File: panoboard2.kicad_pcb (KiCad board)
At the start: 2 copper layers, 100 x 69.6 mm, 69 parts, among them J11 I2C1, J12 I2C2, J2 THERMISTOR, J6 BLK/MAINS L, J7 WHT/HTR, J8 ORA/MAINS N, J9 MOLEX 53375-0810, K1 Relay_SPDT, M2 TINYPICO, P2 PCB_Patch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

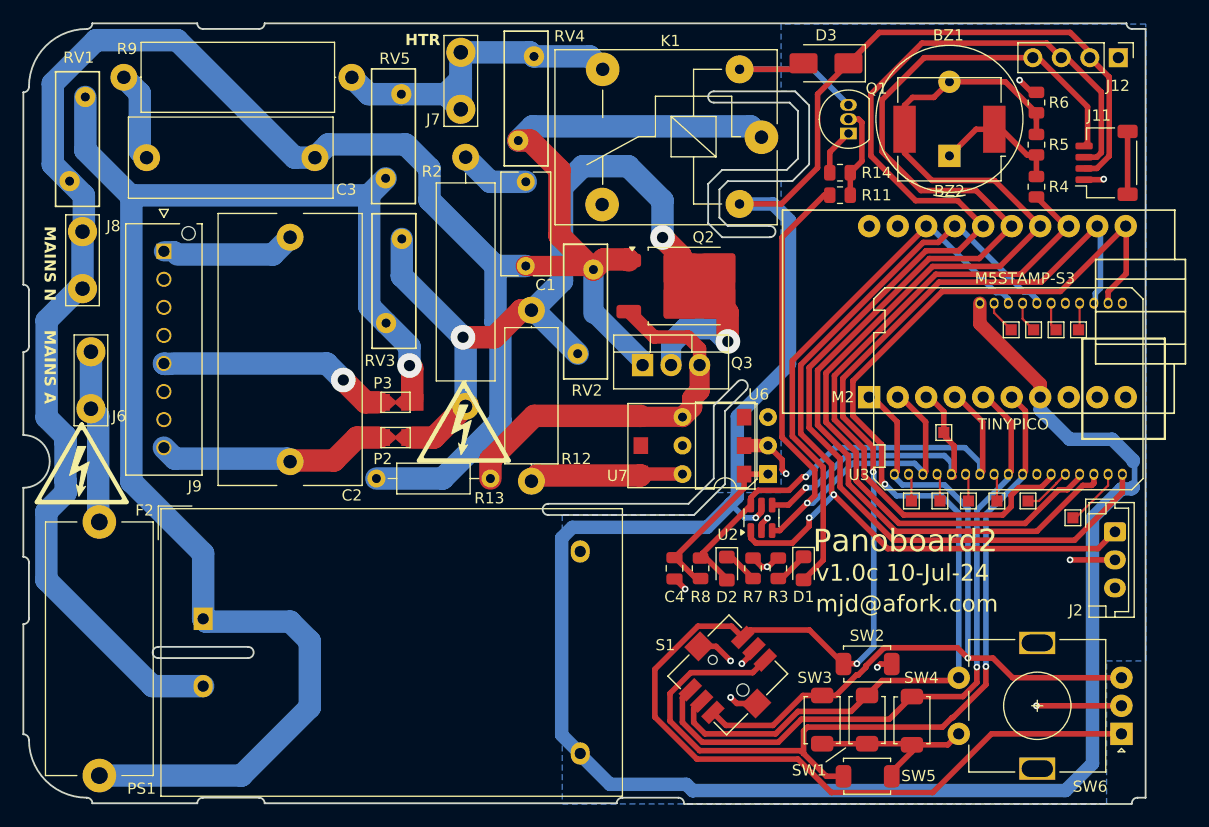
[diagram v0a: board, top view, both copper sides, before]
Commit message: Many improvements
Moved fuse to the neutral line so heater is protected
Added slot under R2
Moved mounting hole
Improved board outline
Added OSHW licence and KiCad shout-out
Fixed buzzer pin pitch
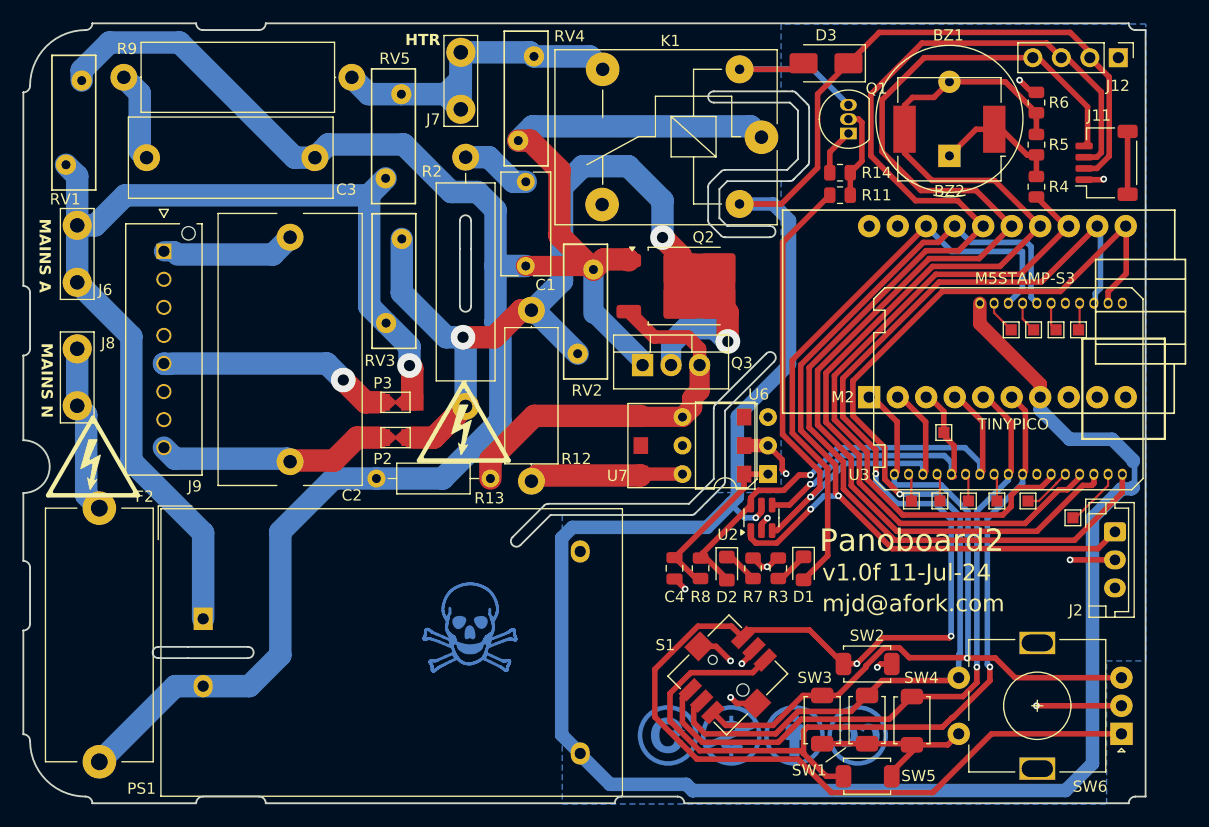
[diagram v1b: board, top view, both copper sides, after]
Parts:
- added REF**: Symbol_CC-Noncommercial_CopperTop_Small, Symbol:Symbol_CC-Noncommercial_CopperTop_Small, B.Cu at (113.1, 93.5)
- added REF**: Symbol_CC-Attribution_CopperTop_Small, Symbol:Symbol_CC-Attribution_CopperTop_Small, B.Cu at (118.7, 93.5)
- added REF**: Symbol_CC-ShareAlike_CopperTop_Small, Symbol:Symbol_CC-ShareAlike_CopperTop_Small, B.Cu at (107.5, 93.5)
- added REF**: OSHW-Logo_5.7x6mm_SilkScreen, Symbol:OSHW-Logo_5.7x6mm_SilkScreen, B.Cu at (107.9, 83.3)
- added REF**: Symbol_Danger_8x8mm_Copper, Symbol:Symbol_Danger_8x8mm_Copper, B.Cu at (89.8, 83.8)
- added REF**: KiCad-Logo2_6mm_SilkScreen, local:KiCad-Logo2_6mm_SilkScreen, B.Cu at (119.7, 83.9)
- added REF**: Symbol_CreativeCommons_CopperTop_Type2_Small, Symbol:Symbol_CreativeCommons_CopperTop_Type2_Small, B.Cu at (124.3, 93.5)
- moved REF** 25.6 mm to (66.0, 74.3)
- moved J6 11.3 mm to (54.8, 48.0)
- moved J8 10.5 mm to (54.8, 59.0)
- moved RV1 6.28 mm to (53.8, 42.6), turned to 90 degrees
- moved F2 1.23 mm to (56.8, 73.2)
- moved REF** 1.17 mm to (56.2, 68.6)
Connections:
- F2 pad 1: Net-(J6-Pin_1) -> Net-(J8-Pin_1)
- F2 pad 2: MAINS_A -> MAINS_N
- J6 pad 1: Net-(J6-Pin_1) -> MAINS_A
- J8 pad 1: MAINS_N -> Net-(J8-Pin_1)
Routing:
- net MAINS_A: track 131.5 -> 94.6 mm
- net MAINS_N: track 206.0 -> 180.2 mm
- net Net-(J6-Pin_1): track 15.5 -> 0.00 mm
- net Net-(J8-Pin_1): track 0.00 -> 15.0 mm
- net /SW2: track 135.0 -> 146.2 mm, vias 2 -> 3
- net /LED: track 48.7 -> 53.3 mm
- net /THERM: track 80.1 -> 82.3 mm
- net /MTR_N: track 77.8 -> 78.6 mm
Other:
- board size 100 x 69.6 mm -> 100 x 69.5 mm
- board text added: ":-)"
- board text added: "CC BY-NC-SA 4.0"
- board text added: "v1.0f 11-Jul-24"
- board text removed: "v1.0c 10-Jul-24"

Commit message: Removed a rebate because there's a support under it.
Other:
- outline, holes or cut-outs redrawn
- board text added: "v1.0g 11-Jul-24"
- board text removed: "v1.0f 11-Jul-24"

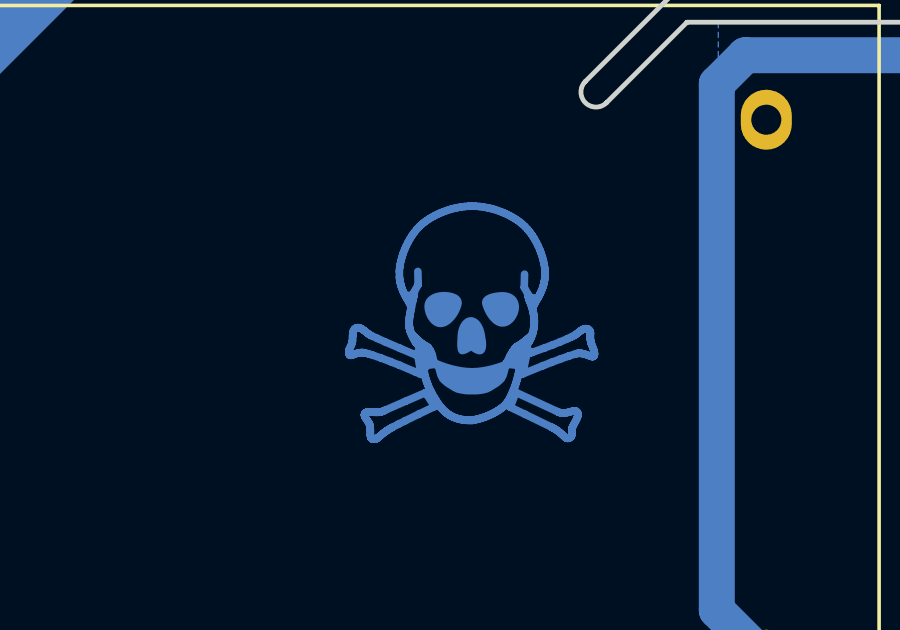
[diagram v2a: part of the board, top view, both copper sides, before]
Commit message: Moved soldermask no-mans-land to match new slots.
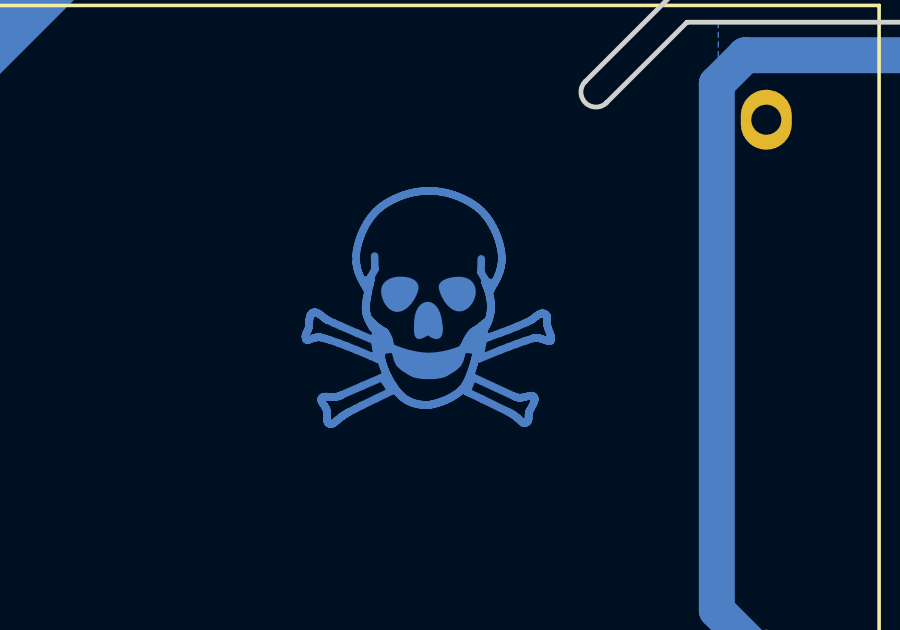
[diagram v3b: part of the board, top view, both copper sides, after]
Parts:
- moved REF** 1.53 mm to (88.4, 83.2)
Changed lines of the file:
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@@
 			(usegerberattributes yes)
 			(usegerberadvancedattributes yes)
-			(creategerberjobfile yes)
+			(creategerberjobfile no)
 			(dashed_line_dash_ratio 12.000000)
 			(dashed_line_gap_ratio 3.000000)
@@
 	(footprint "Symbol:Symbol_Danger_8x8mm_Copper"
 		(layer "B.Cu")
-		(at 89.813608 83.75865 180)
+		(at 88.371392 83.248157 180)
 		(descr "Danger symbol, 8x8mm, copper layer")
 		(tags "warning graphic")
@@
 	)
 	(gr_line
-		(start 114.022216 62.310493)
-		(end 116.522216 59.810493)
-		(stroke
-			(width 1)
-			(type default)
-		)
-		(layer "B.Mask")
-	)
-	(gr_line
-		(start 96.772216 99.560493)
-		(end 96.772216 73.310493)
+		(start 93.97 99.51)
+		(end 93.97 76.18)
 		(stroke
 			(width 1)
@@
 	)
 	(gr_line
-		(start 96.772216 99.560493)
-		(end 96.772216 73.310493)
+		(start 93.97 99.51)
+		(end 93.97 76.18)
 		(stroke
 			(width 1)
@@
 	)
 	(gr_line
-		(start 114.022216 62.310493)
-		(end 116.522216 59.810493)
-		(stroke
-			(width 1)
-			(type default)
-		)
-		(layer "F.Mask")
-	)
-	(gr_line
 		(start 111.522216 36.560493)
 		(end 111.522216 30.060493)
@@
 	)
 	(gr_text "Uncertified design.\nContact with mains voltage may cause death.\nLive board, exercise caution."
-		(at 94.272216 95.560493 0)
+		(at 92.83 95.05 0)
 		(layer "B.SilkS")
 		(effects

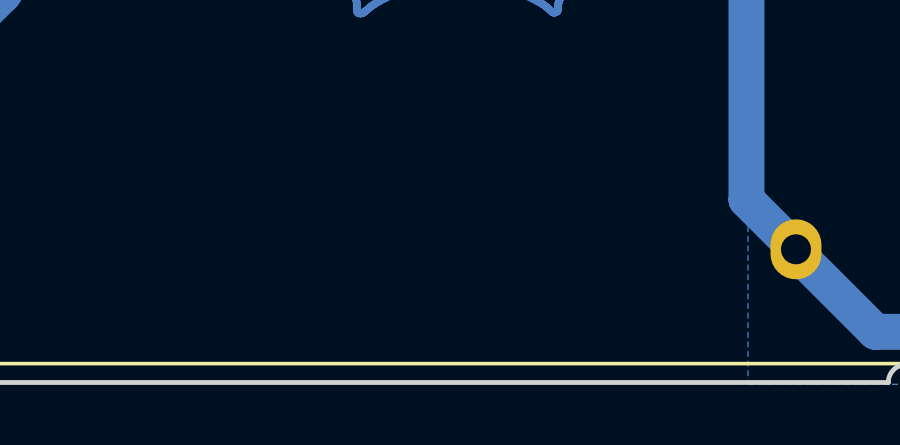
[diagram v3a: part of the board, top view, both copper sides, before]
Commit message: Added JLC production code placement cue
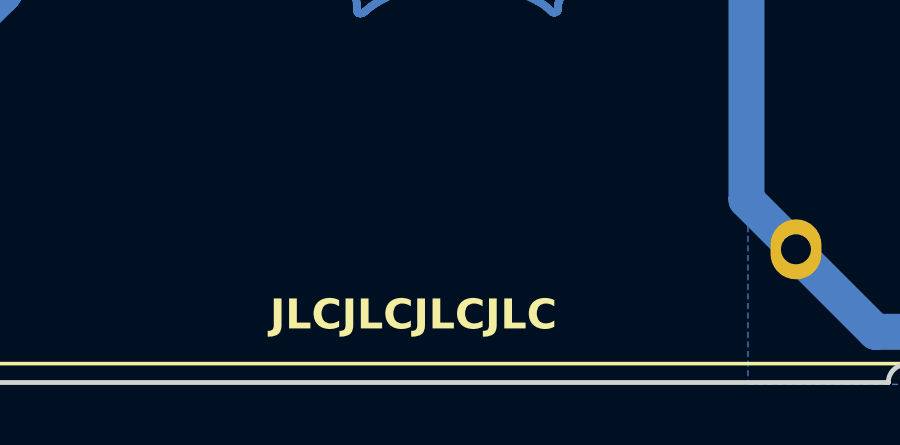
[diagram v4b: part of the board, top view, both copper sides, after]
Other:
- board text added: "JLCJLCJLCJLC"
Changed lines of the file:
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@@
+		)
+	)
+	(gr_text "JLCJLCJLCJLC"
+		(at 82.09 97.82 0)
+		(layer "F.SilkS")
+		(effects
+			(font
+				(size 1 1)
+				(thickness 0.2)
+				(bold yes)
+			)
+			(justify left bottom)
 		)
 	)

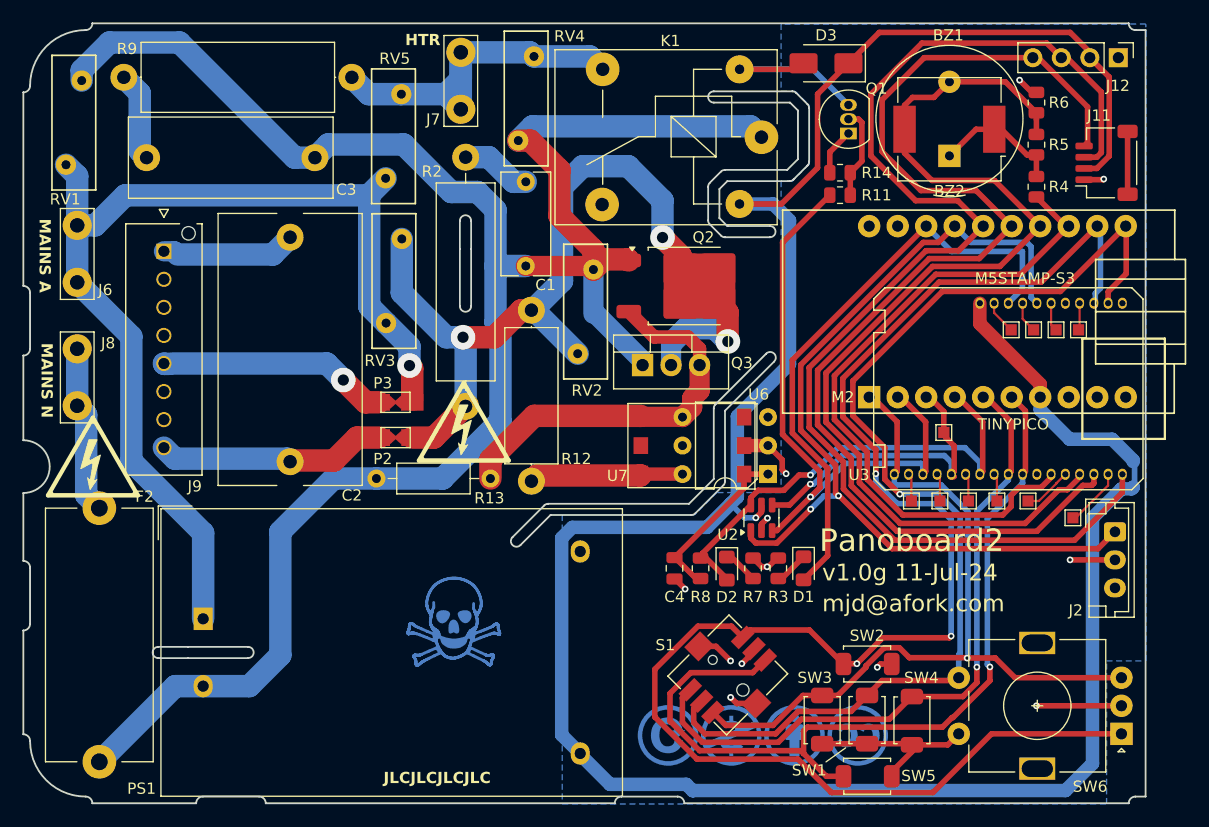
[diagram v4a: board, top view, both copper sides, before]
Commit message: Rotated incorrectly placed motor connector, and added many 3D models.
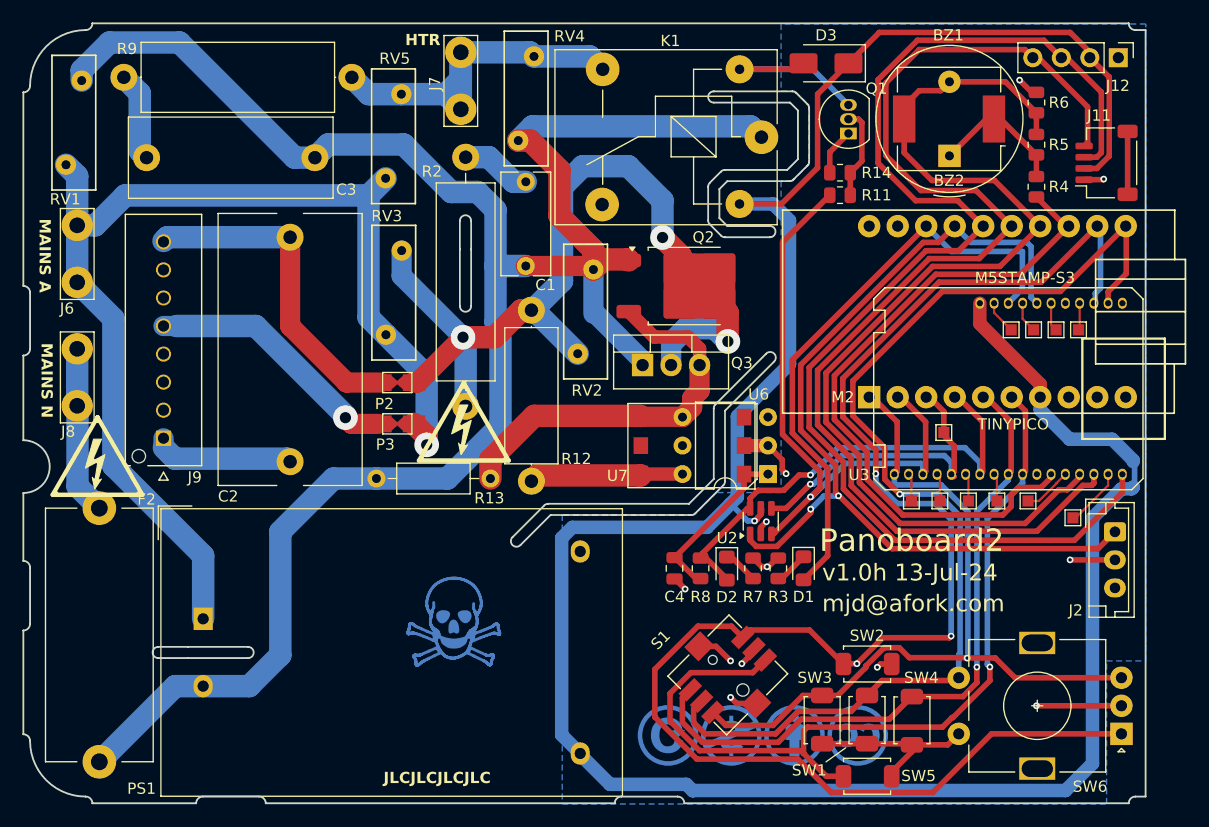
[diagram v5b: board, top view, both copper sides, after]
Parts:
- J6, J7, J8: footprint TestPoint:TestPoint_Bridge_Pitch5.08mm_Drill1.3mm -> local:TE-1742361-1-QC-Tab
- S1: value JS1400BFQ -> SKRHABE010; footprint local:SW_JS1400BFQ -> local:SKRHABE010
- moved C2 20.0 mm to (73.8, 69.1), turned to 90 degrees
- moved J9 16.7 mm to (62.5, 67.0), turned to -90 degrees
- moved P2 4.90 mm to (83.3, 62.0)
- moved P3 1.93 mm to (83.3, 65.7)
- moved RV3 1.04 mm to (82.3, 57.8)
- moved BZ2 0.92 mm to (132.5, 38.5)
- moved REF** 0.41 mm to (56.6, 68.5)
- moved U2 0.31 mm to (115.7, 74.4)
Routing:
- net Net-(J9-Pin_8): track 20.6 -> 29.5 mm
- net MAINS_A: track 94.6 -> 101.4 mm
- net Net-(J9-Pin_5): track 20.2 -> 22.8 mm
- net /MTR_N: track 78.6 -> 76.9 mm
- net /SCL: track 104.2 -> 105.2 mm
- net Net-(BZ1-+): track 11.6 -> 12.4 mm
- net Net-(J9-Pin_1): track 12.0 -> 12.6 mm
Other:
- board text added: "v1.0h 13-Jul-24"
- board text removed: "v1.0g 11-Jul-24"
